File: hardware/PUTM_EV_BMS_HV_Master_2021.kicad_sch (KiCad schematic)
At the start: 22 parts, among them SW1 RESET, U19 STM32F446RETx, Y1 20MHz, Y2 32.768kHz

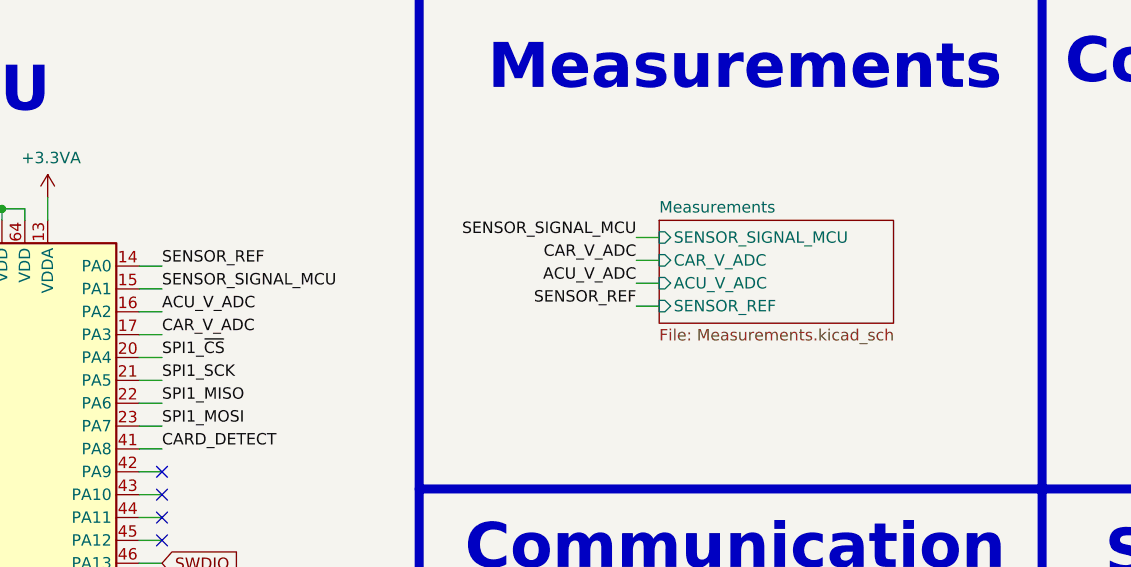
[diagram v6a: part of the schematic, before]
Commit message: remade pcb so it fits into 100 x 100 mm and some minor modifications
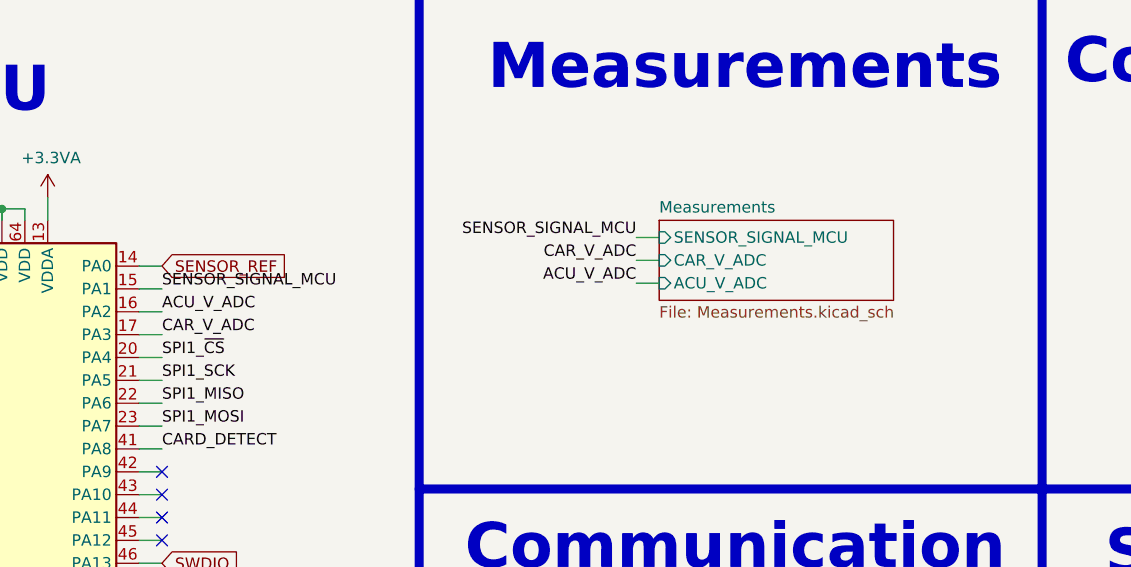
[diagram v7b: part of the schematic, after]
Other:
- sheet Measurements ports: added none; removed SENSOR_REF
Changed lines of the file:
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@@
-    (stroke (width 0) (type default) (color 0 0 0 0))
-  )
-  (wire (pts (xy 131.445 46.355) (xy 133.985 46.355))
     (stroke (width 0) (type default) (color 0 0 0 0))
   )
@@
     (effects (font (size 1.27 1.27)) (justify right bottom))
   )
-  (label "SENSOR_REF" (at 131.445 46.355 180)
-    (effects (font (size 1.27 1.27)) (justify right bottom))
-  )
   (label "DIN_1_MCU" (at 78.74 97.79 0)
     (effects (font (size 1.27 1.27)) (justify left bottom))
@@
   (label "MASTER_MODE" (at 194.945 95.885 180)
     (effects (font (size 1.27 1.27)) (justify right bottom))
-  )
-  (label "SENSOR_REF" (at 78.74 41.91 0)
-    (effects (font (size 1.27 1.27)) (justify left bottom))
   )
   (label "SPI1_~{CS}" (at 248.285 33.655 180)
@@
     (effects (font (size 1.27 1.27)) (justify left))
     (property "Intersheet References" "${INTERSHEET_REFS}" (id 0) (at 87.2932 77.3906 0)
+      (effects (font (size 1.27 1.27)) (justify left) hide)
+    )
+  )
+  (global_label "SENSOR_REF" (shape input) (at 78.74 41.91 0) (fields_autoplaced)
+    (effects (font (size 1.27 1.27)) (justify left))
+    (property "Intersheet References" "${INTERSHEET_REFS}" (id 0) (at 93.0385 41.8306 0)
       (effects (font (size 1.27 1.27)) (justify left) hide)
     )
@@
     )
   )
-  (sheet (at 133.985 36.83) (size 26.035 11.43) (fields_autoplaced)
+  (sheet (at 133.985 36.83) (size 26.035 8.89) (fields_autoplaced)
     (stroke (width 0.1524) (type solid) (color 0 0 0 0))
     (fill (color 0 0 0 0.0000))
@@
       (effects (font (size 1.27 1.27)) (justify left bottom))
     )
-    (property "Sheet file" "Measurements.kicad_sch" (id 1) (at 133.985 48.8446 0)
+    (property "Sheet file" "Measurements.kicad_sch" (id 1) (at 133.985 46.3046 0)
       (effects (font (size 1.27 1.27)) (justify left top))
     )
@@
       (effects (font (size 1.27 1.27)) (justify left))
     )
-    (pin "SENSOR_REF" input (at 133.985 46.355 180)
-      (effects (font (size 1.27 1.27)) (justify left))
-    )

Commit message: schematic override, just cuz
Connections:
- net MCU_D-: now reaches U19.44 (PA11)
- net MCU_D+: now reaches U19.45 (PA12)
- net MCU_UART_RX: no longer names the net of U19.59 (PB7)
- net MCU_UART_TX: no longer names the net of U19.58 (PB6)
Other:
- sheet Communication ports: added MCU_D+, MCU_D-; removed MCU_UART_RX, MCU_UART_TX
